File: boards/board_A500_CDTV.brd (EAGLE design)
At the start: 22.5 x 54.6 mm, 3 parts

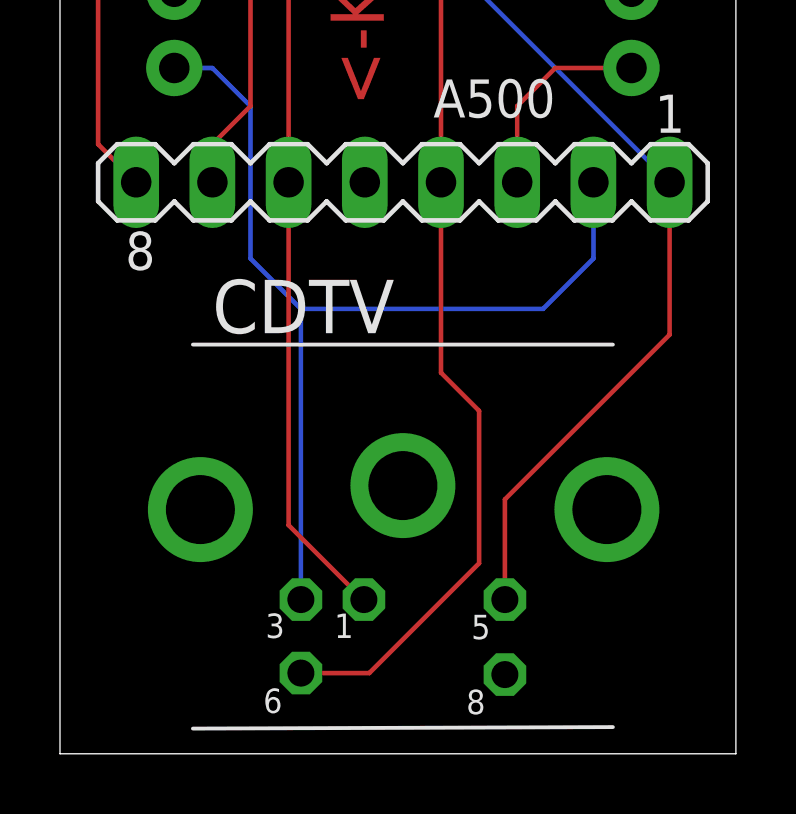
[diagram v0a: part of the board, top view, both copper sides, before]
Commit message: fix socket orientation
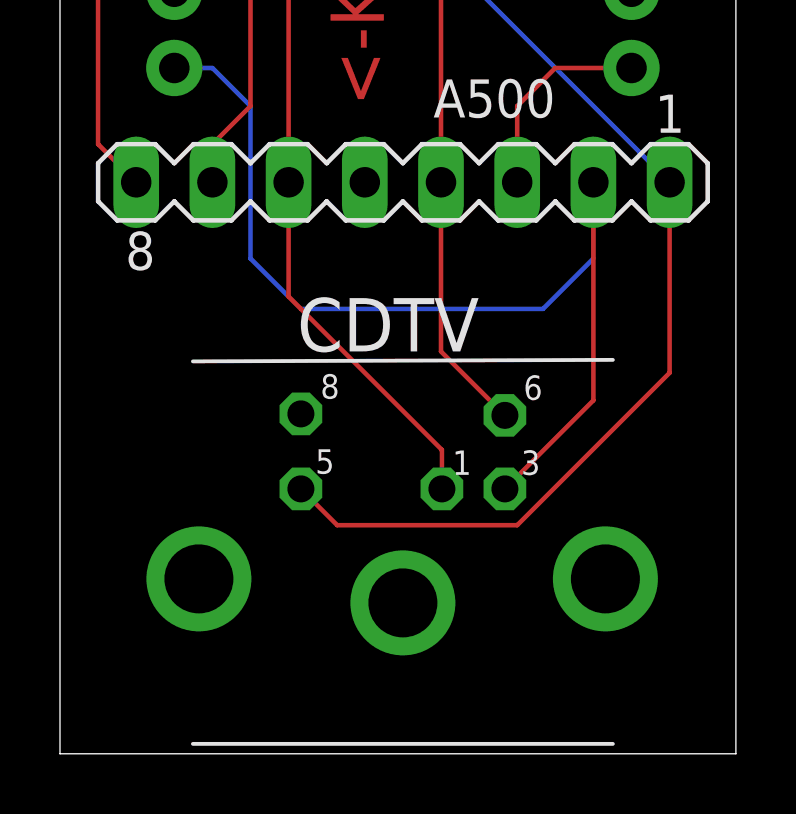
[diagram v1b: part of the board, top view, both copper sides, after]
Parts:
- moved CDTV 3.81 mm to (14.0, 30.5), turned to 180 degrees
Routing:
- net VCC: track 49.7 -> 37.6 mm
- net KBCLK: track 35.3 -> 40.4 mm
- net GND: track 59.5 -> 56.9 mm
- net KBDATA: track 33.2 -> 34.9 mm
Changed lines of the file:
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@@
 <attribute name="VALUE" x="15.24" y="47.371" size="1.27" layer="27" ratio="10" rot="R180"/>
 </element>
-<element name="CDTV" library="mini_din" package="M_DIN5" value="" x="13.97" y="34.29" smashed="yes">
-<attribute name="NAME" x="7.62" y="39.42" size="1.778" layer="25" ratio="10"/>
-<attribute name="VALUE" x="7.62" y="36.88" size="1.778" layer="27" ratio="10"/>
+<element name="CDTV" library="mini_din" package="M_DIN5" value="" x="13.97" y="30.48" smashed="yes" rot="R180">
+<attribute name="NAME" x="16.51" y="40.59" size="1.778" layer="25" ratio="10" rot="R180"/>
+<attribute name="VALUE" x="20.32" y="27.89" size="1.778" layer="27" ratio="10" rot="R180"/>
 </element>
 </elements>
@@
 <wire x1="10.16" y1="64.77" x2="10.16" y2="44.45" width="0.1524" layer="1"/>
 <contactref element="CDTV" pad="1"/>
-<wire x1="10.16" y1="44.45" x2="10.16" y2="33.02" width="0.1524" layer="1"/>
-<wire x1="10.16" y1="33.02" x2="12.64" y2="30.54" width="0.1524" layer="1"/>
-<wire x1="12.64" y1="30.54" x2="12.67" y2="30.54" width="0.1524" layer="1"/>
+<wire x1="15.27" y1="34.23" x2="15.27" y2="35.53" width="0.1524" layer="1"/>
+<wire x1="15.27" y1="35.53" x2="10.16" y2="40.64" width="0.1524" layer="1"/>
+<wire x1="10.16" y1="40.64" x2="10.16" y2="44.45" width="0.1524" layer="1"/>
 </signal>
 <signal name="KBCLK">
@@
 <wire x1="16.51" y1="50.8" x2="22.86" y2="44.45" width="0.1524" layer="16"/>
 <contactref element="CDTV" pad="5"/>
-<wire x1="22.86" y1="44.45" x2="22.86" y2="39.37" width="0.1524" layer="1"/>
-<wire x1="17.37" y1="33.88" x2="17.37" y2="30.54" width="0.1524" layer="1"/>
-<wire x1="22.86" y1="39.37" x2="17.37" y2="33.88" width="0.1524" layer="1"/>
+<wire x1="10.57" y1="34.23" x2="11.78" y2="33.02" width="0.1524" layer="1"/>
+<wire x1="11.78" y1="33.02" x2="17.78" y2="33.02" width="0.1524" layer="1"/>
+<wire x1="17.78" y1="33.02" x2="22.86" y2="38.1" width="0.1524" layer="1"/>
+<wire x1="22.86" y1="38.1" x2="22.86" y2="44.45" width="0.1524" layer="1"/>
 </signal>
 <signal name="KBDATA">
@@
 <wire x1="20.32" y1="44.45" x2="20.32" y2="41.91" width="0.1524" layer="16"/>
 <wire x1="8.89" y1="46.99" x2="8.89" y2="41.91" width="0.1524" layer="16"/>
-<wire x1="10.57" y1="30.54" x2="10.57" y2="40.23" width="0.1524" layer="16"/>
 <wire x1="20.32" y1="41.91" x2="18.64" y2="40.23" width="0.1524" layer="16"/>
 <wire x1="18.64" y1="40.23" x2="10.57" y2="40.23" width="0.1524" layer="16"/>
+<wire x1="17.37" y1="34.23" x2="20.32" y2="37.18" width="0.1524" layer="1"/>
+<wire x1="20.32" y1="37.18" x2="20.32" y2="44.45" width="0.1524" layer="1"/>
 </signal>
 <signal name="VCC">
@@
 <wire x1="17.78" y1="68.58" x2="21.59" y2="68.58" width="0.1524" layer="1"/>
 <contactref element="CDTV" pad="6"/>
-<wire x1="15.24" y1="44.45" x2="15.24" y2="38.1" width="0.1524" layer="1"/>
-<wire x1="15.24" y1="38.1" x2="16.51" y2="36.83" width="0.1524" layer="1"/>
-<wire x1="16.51" y1="36.83" x2="16.51" y2="31.75" width="0.1524" layer="1"/>
-<wire x1="12.85" y1="28.09" x2="10.57" y2="28.09" width="0.1524" layer="1"/>
-<wire x1="16.51" y1="31.75" x2="12.85" y2="28.09" width="0.1524" layer="1"/>
+<wire x1="15.24" y1="44.45" x2="15.24" y2="38.81" width="0.1524" layer="1"/>
+<wire x1="15.24" y1="38.81" x2="17.37" y2="36.68" width="0.1524" layer="1"/>
 </signal>
 <signal name="STATUS">
